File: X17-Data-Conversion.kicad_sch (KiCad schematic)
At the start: 20 parts, among them J1 Conn_01x05, J2 BG030_-_-_-_6_-_-_X_-_XXX_-_-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, J3 BG030_-_-_-_6_-_-_X_-_XXX_-_-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, SW1 1825910-6, U1 ABLS-8.000MHZ-B2-T, U2 STM32F091CCTx

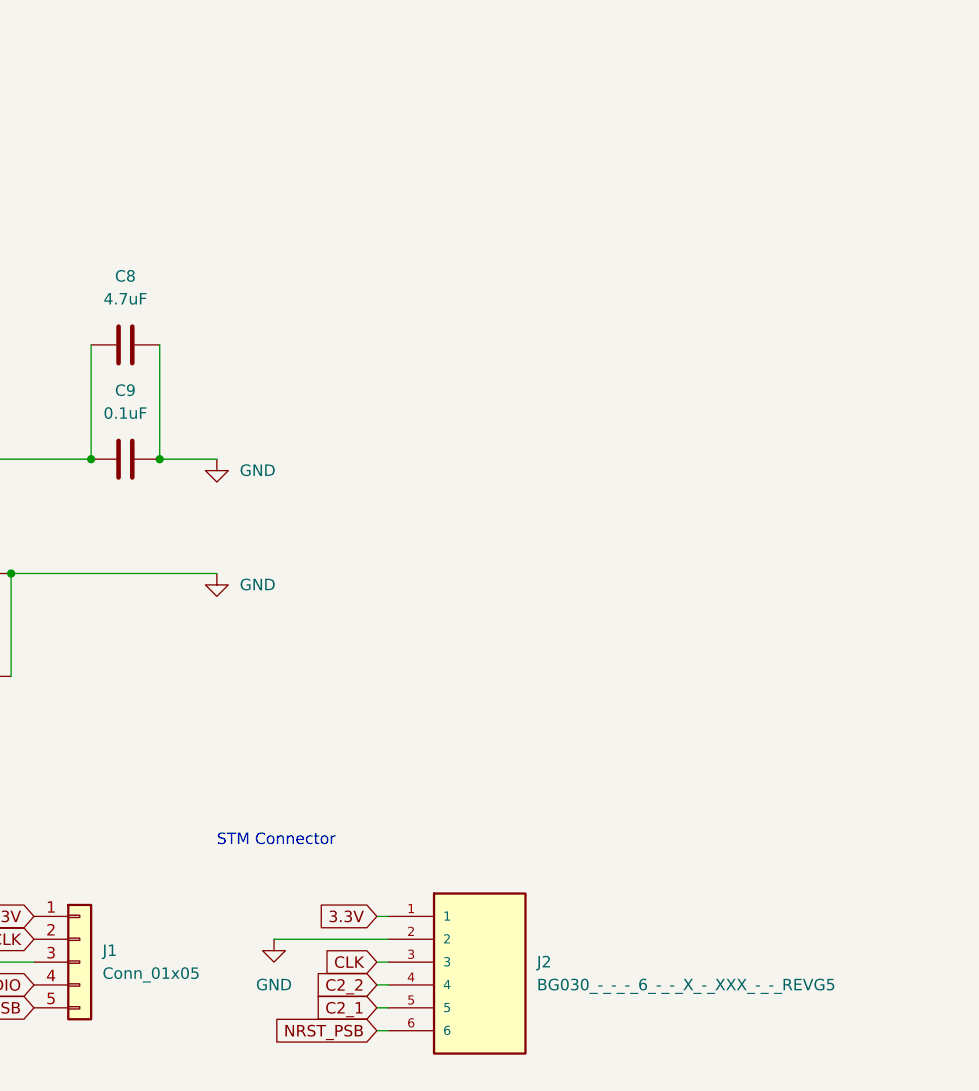
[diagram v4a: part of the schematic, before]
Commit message: Redid to meet specifications no drcs
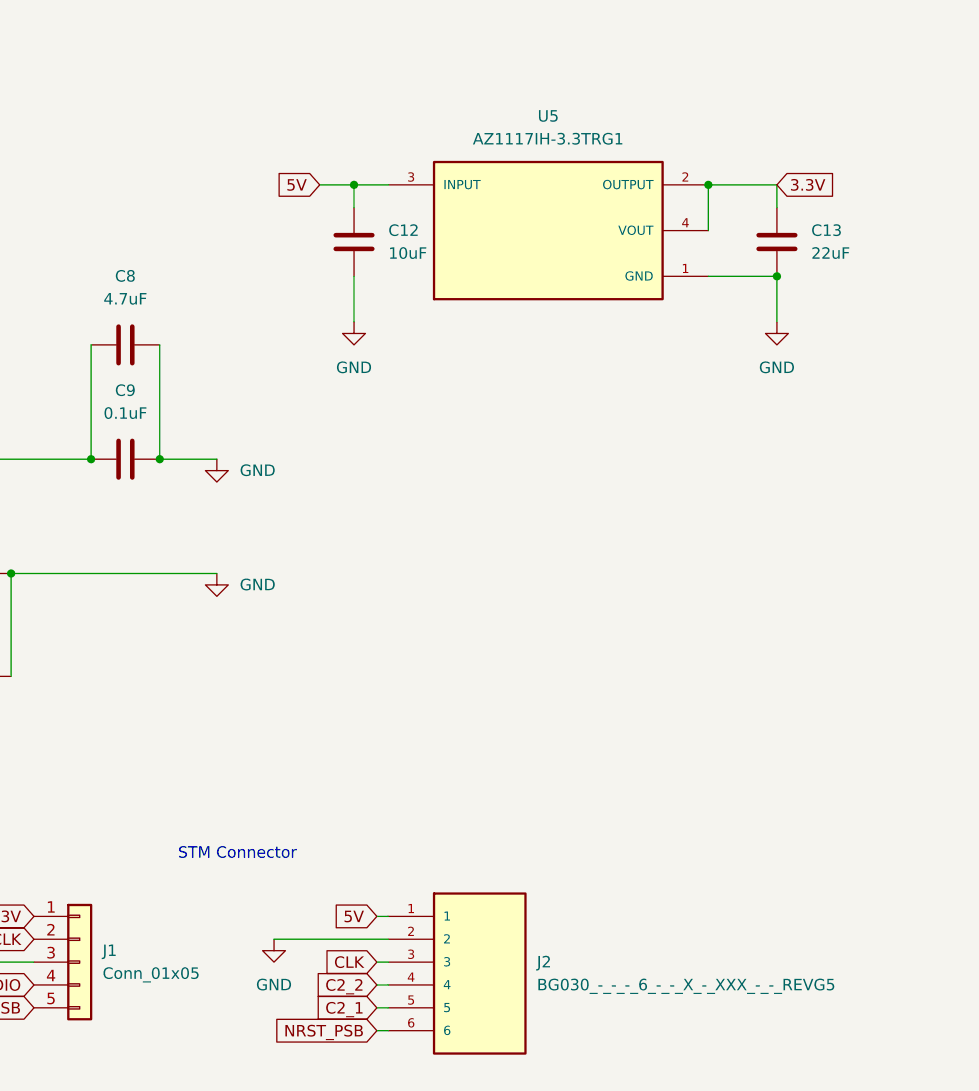
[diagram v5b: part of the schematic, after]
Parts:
- added C12: 10uF, Capacitor_SMD:C_0603_1608Metric_Pad1.08x0.95mm_HandSolder, symbol Device:C
- added C13: 22uF, Capacitor_SMD:C_0603_1608Metric_Pad1.08x0.95mm_HandSolder, symbol Device:C
- added U5: AZ1117IH-3.3TRG1, AZ1117IH_3_3TRG1:SOT230P700X185-4N, symbol AZ1117IH-3.3TRG1:AZ1117IH-3.3TRG1
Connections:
- net 3.3V: now also C13.1, U5.2 (OUTPUT), U5.4 (VOUT); no longer J2.1
- net GND: now also C12.1, C13.2, U5.1 (GND)
- new net 5V: C12.2, J2.1, U5.3 (INPUT)

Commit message: meeting today, need to rewire
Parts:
- removed C2, C3: 18pF, Capacitor_SMD:C_0603_1608Metric_Pad1.08x0.95mm_HandSolder, symbol Device:C
- removed J2, J3: BG030_-_-_-_6_-_-_X_-_XXX_-_-_REVG5, 61300611121:61300611121, symbol BG030_-_-_-_6_-_-_X_-_XXX_-_-_REVG5:BG030_-_-_-_6_-_-_X_-_XXX_-_-_REVG5
- removed R1: 10k, Resistor_SMD:R_0603_1608Metric_Pad0.98x0.95mm_HandSolder, symbol Device:R_US
- removed R3: 4.7k, Resistor_SMD:R_0603_1608Metric_Pad0.98x0.95mm_HandSolder, symbol Device:R_US
- removed SW1: 1825910-6, footprints1:SW4_1825910-B_TEC, symbol STM Switch Symbol:1825910-6
- removed U1: ABLS-8.000MHZ-B2-T, footprints2:ABLS-8.000MHZ-B2-T_ABR, symbol STM32_Oscillator:ABLS-8.000MHZ-B2-T
- added D2: LED, LED_SMD:LED_0805_2012Metric_Pad1.15x1.40mm_HandSolder, symbol Device:LED
- added J4: Conn_01x12_Pin, Library:Data Conversion two 1x6, symbol Connector:Conn_01x12_Pin
- added U4: MAX7375AXR805+T, 21-0075D_MXM, symbol 2024-12-30_21-17-45:MAX7375AXR805+T
- R2: value 4.7k -> 470
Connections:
- net 3.3V: now also C1.1, U4.1 (V+)
- net 5V: now also J4.7 (Pin_7)
- net ALERT1: now also J4.5 (Pin_5)
- net CLK: now also J4.9 (Pin_9); no longer U2.30 (PA9)
- net DATA: now also J4.2 (Pin_2); no longer U2.31 (PA10)
- net GND: now also D2.1 (K), J4.1 (Pin_1), J4.8 (Pin_8), U4.3 (GND)
- net NRST_PSB: now also J4.12 (Pin_12); no longer C1.1
- net SWCLK: now also J4.4 (Pin_4)
- net SWDIO: now also J4.3 (Pin_3)
- net PG: now reaches U2.13 (PA3)
- net PG: now also R2.1, J4.6 (Pin_6)
- net at U2.18 (PB0): no longer R2.1
- net USART1_DE: now reaches U2.33 (PA12)
- net I2C1_SMBA: now reaches U2.41 (PB5)
- net USART1_TX: now reaches U2.42 (PB6)
- net USART1_RX: now reaches U2.43 (PB7)
- net ADC_IN0: no longer names the net of U2.15 (PA5)
- net ADC_IN1: no longer names the net of U2.14 (PA4)
- net ADC_IN2: no longer names the net of U2.16 (PA6)
- net ALERT2: no longer names the net of U2.39 (PB3)
- net C2_1: no longer names the net of R2.2
- net C2_1: now also D2.2 (A)
- net OSC_IN: no longer names the net of U2.5 (PF0)
- net OSC_IN: now also U4.2 (CLOCK)
- net OSC_OUT: no longer names the net of U2.6 (PF1)
- new net A+: J4.10 (Pin_10)
- new net A-: J4.11 (Pin_11)
- new net I2C1_SCL: U2.30 (PA9)
- new net I2C1_SDA: U2.31 (PA10)
- no-connect marks 23 -> 25

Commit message: hny!
lookinggood, happy new year!
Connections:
- net CLK is gone; now on net I2C1_SCL: J4.9 (Pin_9)
- net DATA is gone; now on net I2C1_SDA: J4.2 (Pin_2)
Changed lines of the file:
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@@
 		)
 	)
-	(global_label "DATA"
+	(global_label "I2C1_SDA"
 		(shape input)
 		(at 238.76 123.19 180)
@@
 		)
 		(property "Intersheetrefs" "${INTERSHEET_REFS}"
-			(at 231.36 123.19 0)
+			(at 226.9453 123.19 0)
 			(effects
 				(font
@@
 		)
 	)
-	(global_label "CLK"
+	(global_label "I2C1_SCL"
 		(shape input)
 		(at 237.49 140.97 180)
@@
 		)
 		(property "Intersheetrefs" "${INTERSHEET_REFS}"
-			(at 230.9367 140.97 0)
-			(effects
-				(font
+			(at 225.7358 140.97 0)
+			(effects
+				(font

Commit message: daniel lookie
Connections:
- net A+: now also J4.12 (Pin_12); no longer J4.10 (Pin_10)
- net NRST_PSB: now also J4.10 (Pin_10); no longer J4.12 (Pin_12)
- net SWCLK: no longer J4.4 (Pin_4)
- net SWDIO: no longer J4.3 (Pin_3)
- no-connect marks 25 -> 27
